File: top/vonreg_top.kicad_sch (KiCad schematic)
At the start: 17 parts, among them K1 SW_Push, K10 SW_Push, K11 SW_Push, K12 SW_Push, K15 SW_Push, K2 SW_Push, K3 SW_Push, K4 SW_Push, K5 SW_Push, K6 SW_Push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

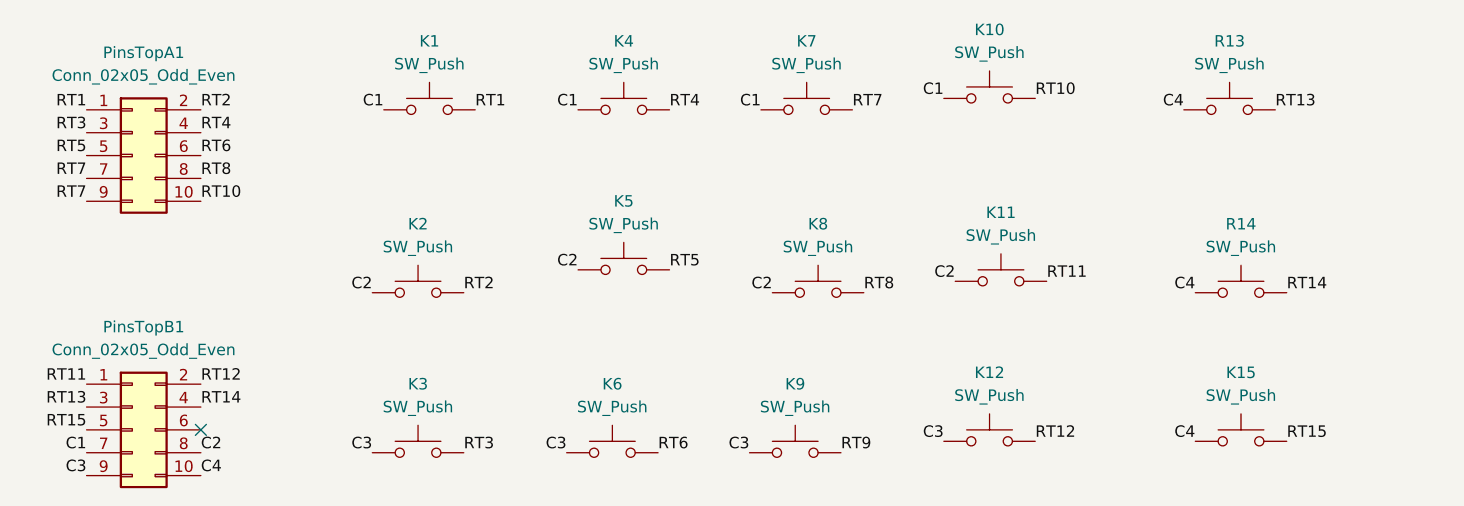
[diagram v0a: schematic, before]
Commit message: Aligned top/bottom
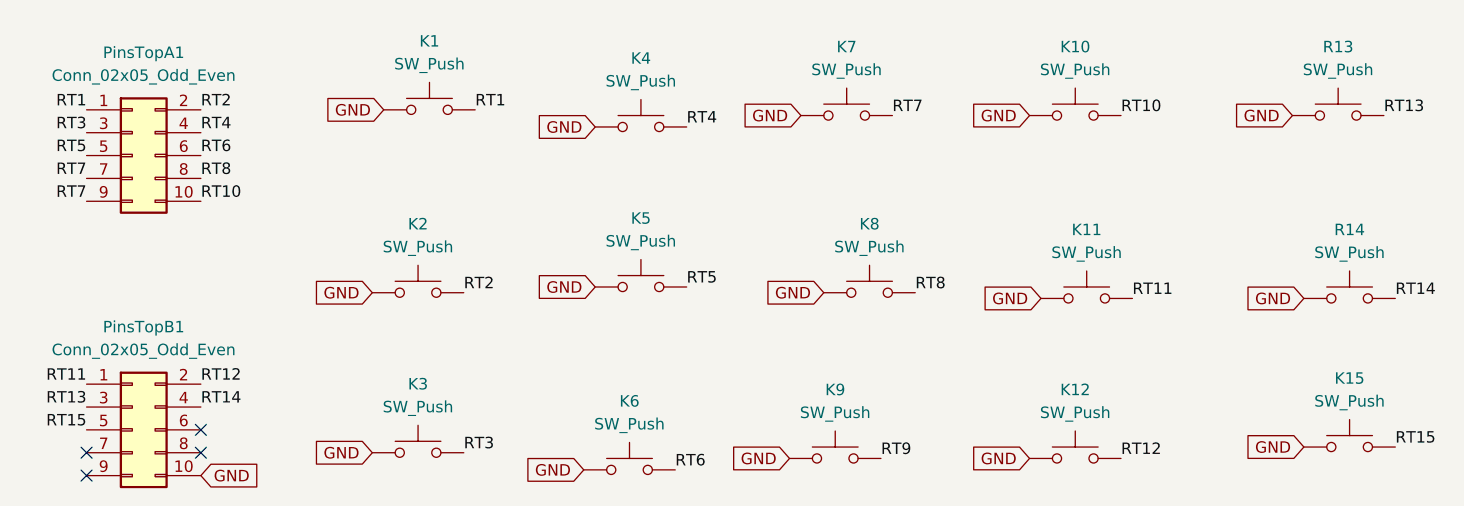
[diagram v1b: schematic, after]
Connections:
- net C4 is gone; now on net GND: K15.1, PinsTopB1.10 (Pin_10), R13.1, R14.1
- net C1 renamed GND
- net GND: now also K11.1, K12.1, K2.1, K3.1, K5.1, K6.1, K8.1, K9.1; no longer PinsTopB1.7 (Pin_7)
- removed net C2: K11.1, K2.1, K5.1, K8.1, PinsTopB1.8 (Pin_8)
- removed net C3: K12.1, K3.1, K6.1, K9.1, PinsTopB1.9 (Pin_9)
- no-connect marks 1 -> 4
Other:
- moved on the sheet: K10, K11, K12, K15, K4, K5, K6, K7, K8, K9, R13, R14

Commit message: Routing done, hopefully
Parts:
- K1, K10, K11, K12, K15, K2, K3, K4, K5, K6, K7, K8, K9, R13, R14: footprint Button_Switch_Keyboard:SW_Cherry_MX_1.00u_PCB -> Button_Switch_Keyboard:Kailh_socket_MX_optional_reversible
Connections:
- net GND: now also PinsTopB1.4 (Pin_4); no longer PinsTopB1.10 (Pin_10)
- net RT1: now also PinsTopA1.6 (Pin_6); no longer PinsTopA1.1 (Pin_1)
- net RT10: now also PinsTopA1.9 (Pin_9); no longer PinsTopA1.10 (Pin_10)
- net RT11: now also PinsTopB1.2 (Pin_2); no longer PinsTopB1.1 (Pin_1)
- net RT12: now also PinsTopB1.9 (Pin_9); no longer PinsTopB1.2 (Pin_2)
- net RT13: now also PinsTopA1.4 (Pin_4); no longer PinsTopB1.3 (Pin_3)
- net RT14: now also PinsTopA1.2 (Pin_2); no longer PinsTopB1.4 (Pin_4)
- net RT15: now also PinsTopB1.7 (Pin_7); no longer PinsTopB1.5 (Pin_5)
- net RT2: now also PinsTopB1.5 (Pin_5); no longer PinsTopA1.2 (Pin_2)
- net RT3: now also PinsTopB1.6 (Pin_6); no longer PinsTopA1.3 (Pin_3)
- net RT4: now also PinsTopA1.8 (Pin_8); no longer PinsTopA1.4 (Pin_4)
- net RT5: now also PinsTopB1.3 (Pin_3); no longer PinsTopA1.5 (Pin_5)
- net RT6: now also PinsTopB1.8 (Pin_8); no longer PinsTopA1.6 (Pin_6)
- net RT7: now also PinsTopA1.10 (Pin_10); no longer PinsTopA1.7 (Pin_7), PinsTopA1.9 (Pin_9)
- net RT8: now also PinsTopB1.1 (Pin_1); no longer PinsTopA1.8 (Pin_8)
- net RT9: now also PinsTopB1.10 (Pin_10)

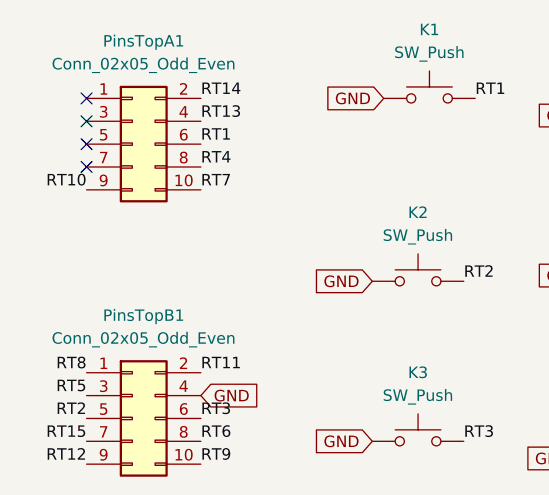
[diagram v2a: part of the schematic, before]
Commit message: Ground pour and buzzer
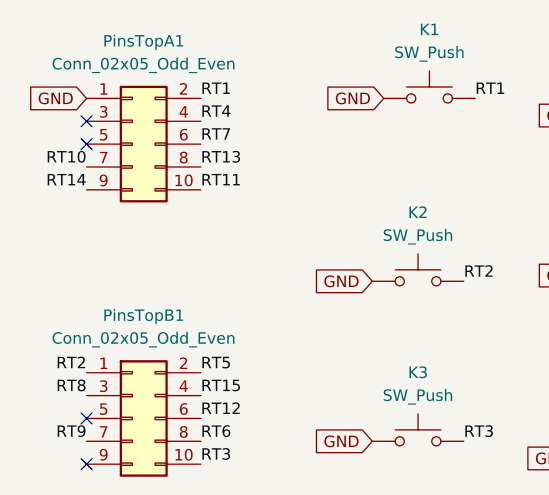
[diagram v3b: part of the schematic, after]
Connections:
- net GND: now also PinsTopA1.1 (Pin_1); no longer PinsTopB1.4 (Pin_4)
- net RT1: now also PinsTopA1.2 (Pin_2); no longer PinsTopA1.6 (Pin_6)
- net RT10: now also PinsTopA1.7 (Pin_7); no longer PinsTopA1.9 (Pin_9)
- net RT11: now also PinsTopA1.10 (Pin_10); no longer PinsTopB1.2 (Pin_2)
- net RT12: now also PinsTopB1.6 (Pin_6); no longer PinsTopB1.9 (Pin_9)
- net RT13: now also PinsTopA1.8 (Pin_8); no longer PinsTopA1.4 (Pin_4)
- net RT14: now also PinsTopA1.9 (Pin_9); no longer PinsTopA1.2 (Pin_2)
- net RT15: now also PinsTopB1.4 (Pin_4); no longer PinsTopB1.7 (Pin_7)
- net RT2: now also PinsTopB1.1 (Pin_1); no longer PinsTopB1.5 (Pin_5)
- net RT3: now also PinsTopB1.10 (Pin_10); no longer PinsTopB1.6 (Pin_6)
- net RT4: now also PinsTopA1.4 (Pin_4); no longer PinsTopA1.8 (Pin_8)
- net RT5: now also PinsTopB1.2 (Pin_2); no longer PinsTopB1.3 (Pin_3)
- net RT7: now also PinsTopA1.6 (Pin_6); no longer PinsTopA1.10 (Pin_10)
- net RT8: now also PinsTopB1.3 (Pin_3); no longer PinsTopB1.1 (Pin_1)
- net RT9: now also PinsTopB1.7 (Pin_7); no longer PinsTopB1.10 (Pin_10)
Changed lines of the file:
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@@
     (company "Appman")
   )
-  (no_connect (at 36.83 46.99))
+  (no_connect (at 36.83 82.55))
   (no_connect (at 36.83 49.53))
   (no_connect (at 36.83 52.07))
-  (no_connect (at 36.83 54.61))
+  (no_connect (at 36.83 87.63))
   (label "RT6" (at 49.53 85.09 0)
     (effects (font (size 1.27 1.27)) (justify left bottom))
@@
     (effects (font (size 1.27 1.27)) (justify left bottom))
   )
-  (label "RT15" (at 36.83 85.09 180)
+  (label "RT9" (at 36.83 85.09 180)
     (effects (font (size 1.27 1.27)) (justify right bottom))
   )
-  (label "RT4" (at 49.53 54.61 0)
+  (label "RT13" (at 49.53 54.61 0)
     (effects (font (size 1.27 1.27)) (justify left bottom))
   )
-  (label "RT11" (at 49.53 77.47 0)
+  (label "RT5" (at 49.53 77.47 0)
     (effects (font (size 1.27 1.27)) (justify left bottom))
   )
@@
     (effects (font (size 1.27 1.27)) (justify left bottom))
   )
-  (label "RT8" (at 36.83 77.47 180)
+  (label "RT2" (at 36.83 77.47 180)
     (effects (font (size 1.27 1.27)) (justify right bottom))
   )
@@
     (effects (font (size 1.27 1.27)) (justify left bottom))
   )
-  (label "RT14" (at 49.53 46.99 0)
+  (label "RT1" (at 49.53 46.99 0)
     (effects (font (size 1.27 1.27)) (justify left bottom))
   )
-  (label "RT12" (at 36.83 87.63 180)
-    (effects (font (size 1.27 1.27)) (justify right bottom))
-  )
-  (label "RT13" (at 49.53 49.53 0)
+  (label "RT4" (at 49.53 49.53 0)
     (effects (font (size 1.27 1.27)) (justify left bottom))
-  )
-  (label "RT2" (at 36.83 82.55 180)
-    (effects (font (size 1.27 1.27)) (justify right bottom))
   )
   (label "RT11" (at 153.035 67.945 0)
@@
     (effects (font (size 1.27 1.27)) (justify left bottom))
   )
-  (label "RT1" (at 49.53 52.07 0)
+  (label "RT7" (at 49.53 52.07 0)
     (effects (font (size 1.27 1.27)) (justify left bottom))
   )
@@
     (effects (font (size 1.27 1.27)) (justify left bottom))
   )
-  (label "RT5" (at 36.83 80.01 180)
+  (label "RT8" (at 36.83 80.01 180)
     (effects (font (size 1.27 1.27)) (justify right bottom))
   )
@@
     (effects (font (size 1.27 1.27)) (justify left bottom))
   )
+  (label "RT15" (at 49.53 80.01 0)
+    (effects (font (size 1.27 1.27)) (justify left bottom))
+  )
   (label "RT3" (at 78.74 85.09 0)
     (effects (font (size 1.27 1.27)) (justify left bottom))
   )
-  (label "RT9" (at 49.53 87.63 0)
+  (label "RT3" (at 49.53 87.63 0)
     (effects (font (size 1.27 1.27)) (justify left bottom))
   )
-  (label "RT3" (at 49.53 82.55 0)
+  (label "RT10" (at 36.83 54.61 180)
+    (effects (font (size 1.27 1.27)) (justify right bottom))
+  )
+  (label "RT12" (at 49.53 82.55 0)
     (effects (font (size 1.27 1.27)) (justify left bottom))
   )
@@
     (effects (font (size 1.27 1.27)) (justify left bottom))
   )
-  (label "RT10" (at 36.83 57.15 180)
+  (label "RT14" (at 36.83 57.15 180)
     (effects (font (size 1.27 1.27)) (justify right bottom))
   )
-  (label "RT7" (at 49.53 57.15 0)
+  (label "RT11" (at 49.53 57.15 0)
     (effects (font (size 1.27 1.27)) (justify left bottom))
   )
-  (global_label "GND" (shape input) (at 49.53 80.01 0) (fields_autoplaced)
-    (effects (font (size 1.27 1.27)) (justify left))
-    (property "Intersheet References" "${INTERSHEET_REFS}" (id 0) (at 55.8136 79.9306 0)
-      (effects (font (size 1.27 1.27)) (justify left) hide)
+  (global_label "GND" (shape input) (at 36.83 46.99 180) (fields_autoplaced)
+    (effects (font (size 1.27 1.27)) (justify right))
+    (property "Intersheet References" "${INTERSHEET_REFS}" (id 0) (at 30.5464 46.9106 0)
+      (effects (font (size 1.27 1.27)) (justify right) hide)
     )
   )
